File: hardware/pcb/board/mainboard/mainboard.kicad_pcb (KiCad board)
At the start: 6 copper layers, 76.4 x 55 mm, 145 parts, among them J1 Conn_Coaxial, J10 USB_C_Receptacle, J11 2908-05WB-MG, J2 USB_C_Receptacle_USB2.0_16P, J3 Conn_02x35_Odd_Even_MountingP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, J4 Conn_02x40_Odd_Even_MountingP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, J5 Conn_02x40_Odd_Even_MountingP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, J7 Conn_01x30, J8 Conn_01x30, Q1 BSS138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

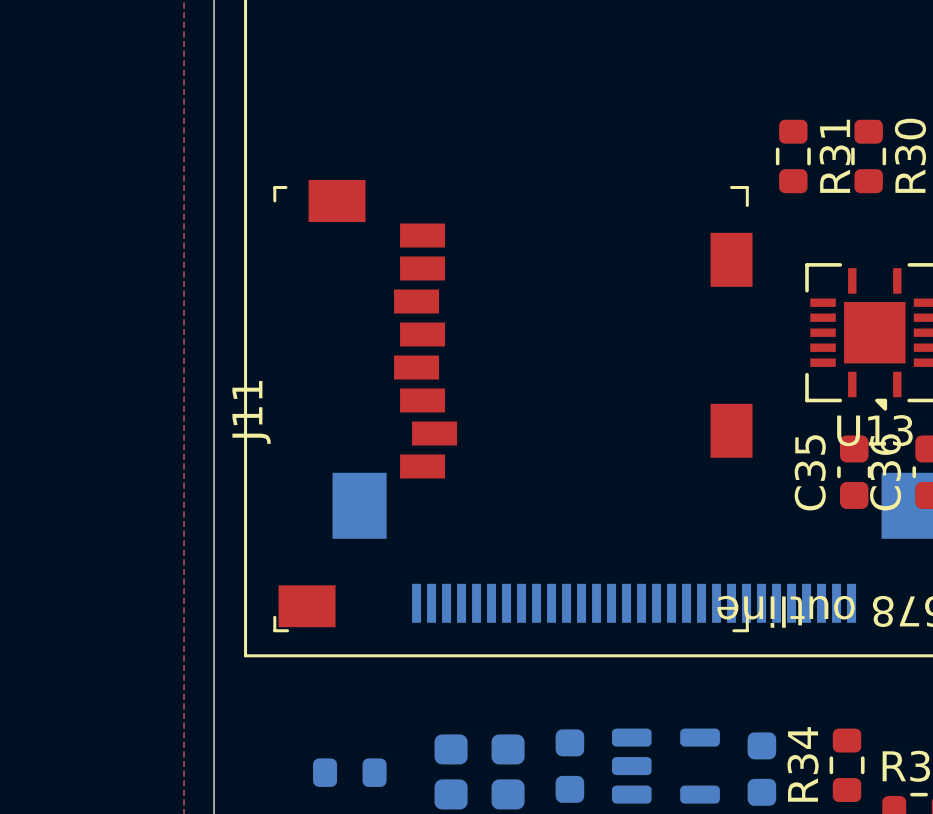
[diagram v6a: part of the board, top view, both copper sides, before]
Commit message: placeholder osci 3d shape
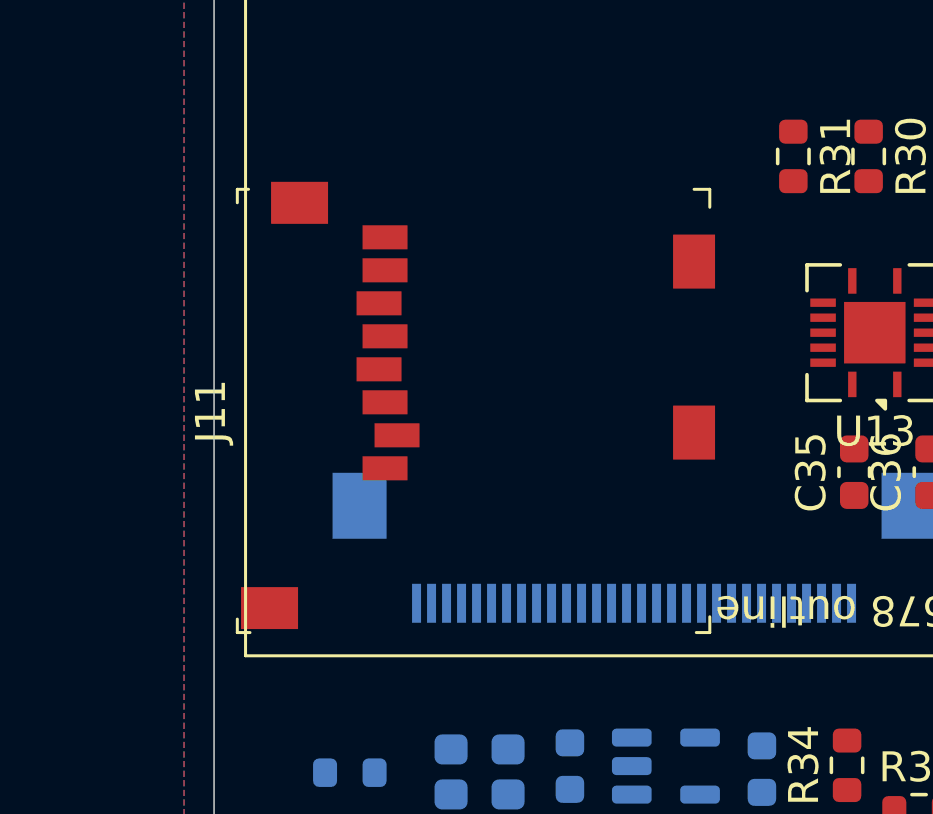
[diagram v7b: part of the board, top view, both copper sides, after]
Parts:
- moved J11 1.25 mm to (105.7, 120.6)
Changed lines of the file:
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@@
 		)
 		(embedded_fonts no)
-		(model "${KICAD10_3DMODEL_DIR}/Oscillator.3dshapes/Oscillator_SMD_SiT_PQFN-4Pin_2.5x2.0mm.step"
+		(model "${KICAD10_3DMODEL_DIR}/Package_DFN_QFN.3dshapes/TDFN-6-1EP_2.5x2.5mm_P0.65mm_EP1.3x2mm.step"
 			(offset
 				(xyz 0 0 0)
@@
 	(footprint "digikey-footprints:MicroSD_2908-05WB-MG"
 		(layer "F.Cu")
-		(at 106.95 120.54 90)
+		(at 105.7 120.6 90)
 		(property "Reference" "J11"
 			(at 1.9 -5.8 90)
@@
 		)
 		(embedded_fonts no)
-		(model "${KICAD10_3DMODEL_DIR}/Oscillator.3dshapes/Oscillator_SMD_SiT_PQFN-4Pin_2.5x2.0mm.step"
+		(model "${KICAD10_3DMODEL_DIR}/Package_DFN_QFN.3dshapes/TDFN-6-1EP_2.5x2.5mm_P0.65mm_EP1.3x2mm.step"
 			(offset
 				(xyz 0 0 0)
@@
 	)
 	(segment
+		(start 150.7 127.6)
+		(end 150.7 128.375)
+		(width 0.2)
+		(layer "F.Cu")
+		(net "VDD_1V8")
+	)
+	(segment
+		(start 150.3 127.55)
+		(end 150.1 127.35)
+		(width 0.2)
+		(layer "F.Cu")
+		(net "VDD_1V8")
+	)
+	(segment
+		(start 150.9 127.4)
+		(end 150.7 127.6)
+		(width 0.2)
+		(layer "F.Cu")
+		(net "VDD_1V8")
+	)
+	(segment
+		(start 130.8 123.6)
+		(end 132.8 125.6)
+		(width 0.2)
+		(layer "F.Cu")
+		(net "VDD_1V8")
+	)
+	(segment
+		(start 130.8 123.075)
+		(end 130.8 123.6)
+		(width 0.2)
+		(layer "F.Cu")
+		(net "VDD_1V8")
+	)
+	(segment
+		(start 130.8 123.075)
+		(end 132.775 123.075)
+		(width 0.2)
+		(layer "F.Cu")
+		(net "VDD_1V8")
+	)
+	(segment
+		(start 136.55 123.075)
+		(end 138.375 123.075)
+		(width 0.2)
+		(layer "F.Cu")
+		(net "VDD_1V8")
+	)
+	(segment
+		(start 138.375 123.075)
+		(end 138.4 123.05)
+		(width 0.2)
+		(layer "F.Cu")
+		(net "VDD_1V8")
+	)
+	(segment
+		(start 132.8 121.7)
+		(end 132.8 123.05)
+		(width 0.2)
+		(layer "F.Cu")
+		(net "VDD_1V8")
+	)
+	(segment
+		(start 150.3 128.375)
+		(end 150.3 127.55)
+		(width 0.2)
+		(layer "F.Cu")
+		(net "VDD_1V8")
+	)
+	(segment
+		(start 133.75 120.35)
+		(end 133.75 120.75)
+		(width 0.2)
+		(layer "F.Cu")
+		(net "VDD_1V8")
+	)
+	(segment
+		(start 132.775 123.075)
+		(end 132.8 123.05)
+		(width 0.2)
+		(layer "F.Cu")
+		(net "VDD_1V8")
+	)
+	(segment
+		(start 136.55 123.075)
+		(end 136.55 124.95)
+		(width 0.2)
+		(layer "F.Cu")
+		(net "VDD_1V8")
+	)
+	(segment
+		(start 133.75 120.75)
+		(end 132.8 121.7)
+		(width 0.2)
+		(layer "F.Cu")
+		(net "VDD_1V8")
+	)
+	(via
+		(at 150.1 127.4)
+		(size 0.45)
+		(drill 0.25)
+		(layers "F.Cu" "B.Cu")
+		(net "VDD_1V8")
+	)
+	(via
+		(at 136.55 124.95)
+		(size 0.45)
+		(drill 0.25)
+		(layers "F.Cu" "B.Cu")
+		(net "VDD_1V8")
+	)
+	(via
+		(at 132.8 125.6)
+		(size 0.45)
+		(drill 0.25)
+		(layers "F.Cu" "B.Cu")
+		(net "VDD_1V8")
+	)
+	(via
+		(at 150.9 127.4)
+		(size 0.45)
+		(drill 0.25)
+		(layers "F.Cu" "B.Cu")
+		(net "VDD_1V8")
+	)
+	(segment
 		(start 145.85 137.675)
 		(end 145.575 137.675)
@@
 	)
 	(segment
-		(start 150.7 127.6)
-		(end 150.7 128.375)
-		(width 0.2)
-		(layer "F.Cu")
-		(net "VDD_1V8")
-	)
-	(segment
-		(start 150.3 127.55)
-		(end 150.1 127.35)
-		(width 0.2)
-		(layer "F.Cu")
-		(net "VDD_1V8")
-	)
-	(segment
-		(start 150.9 127.4)
-		(end 150.7 127.6)
-		(width 0.2)
-		(layer "F.Cu")
-		(net "VDD_1V8")
-	)
-	(segment
-		(start 130.8 123.6)
-		(end 132.8 125.6)
-		(width 0.2)
-		(layer "F.Cu")
-		(net "VDD_1V8")
-	)
-	(segment
-		(start 130.8 123.075)
-		(end 130.8 123.6)
-		(width 0.2)
-		(layer "F.Cu")
-		(net "VDD_1V8")
-	)
-	(segment
-		(start 130.8 123.075)
-		(end 132.775 123.075)
-		(width 0.2)
-		(layer "F.Cu")
-		(net "VDD_1V8")
-	)
-	(segment
-		(start 136.55 123.075)
-		(end 138.375 123.075)
-		(width 0.2)
-		(layer "F.Cu")
-		(net "VDD_1V8")
-	)
-	(segment
-		(start 138.375 123.075)
-		(end 138.4 123.05)
-		(width 0.2)
-		(layer "F.Cu")
-		(net "VDD_1V8")
-	)
-	(segment
-		(start 132.8 121.7)
-		(end 132.8 123.05)
-		(width 0.2)
-		(layer "F.Cu")
-		(net "VDD_1V8")
-	)
-	(segment
-		(start 150.3 128.375)
-		(end 150.3 127.55)
-		(width 0.2)
-		(layer "F.Cu")
-		(net "VDD_1V8")
-	)
-	(segment
-		(start 133.75 120.35)
-		(end 133.75 120.75)
-		(width 0.2)
-		(layer "F.Cu")
-		(net "VDD_1V8")
-	)
-	(segment
-		(start 132.775 123.075)
-		(end 132.8 123.05)
-		(width 0.2)
-		(layer "F.Cu")
-		(net "VDD_1V8")
-	)
-	(segment
-		(start 136.55 123.075)
-		(end 136.55 124.95)
-		(width 0.2)
-		(layer "F.Cu")
-		(net "VDD_1V8")
-	)
-	(segment
-		(start 133.75 120.75)
-		(end 132.8 121.7)
-		(width 0.2)
-		(layer "F.Cu")
-		(net "VDD_1V8")
-	)
-	(via
-		(at 150.1 127.4)
-		(size 0.45)
-		(drill 0.25)
-		(layers "F.Cu" "B.Cu")
-		(net "VDD_1V8")
-	)
-	(via
-		(at 136.55 124.95)
-		(size 0.45)
-		(drill 0.25)
-		(layers "F.Cu" "B.Cu")
-		(net "VDD_1V8")
-	)
-	(via
-		(at 132.8 125.6)
-		(size 0.45)
-		(drill 0.25)
-		(layers "F.Cu" "B.Cu")
-		(net "VDD_1V8")
-	)
-	(via
-		(at 150.9 127.4)
-		(size 0.45)
-		(drill 0.25)
-		(layers "F.Cu" "B.Cu")
-		(net "VDD_1V8")
-	)
-	(segment
